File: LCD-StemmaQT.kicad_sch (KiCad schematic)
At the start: 18 parts, among them J101 StemmaQT, J102 LCD, J103 BL enable, Q101 MMBT3904, U101 PCF8574TS

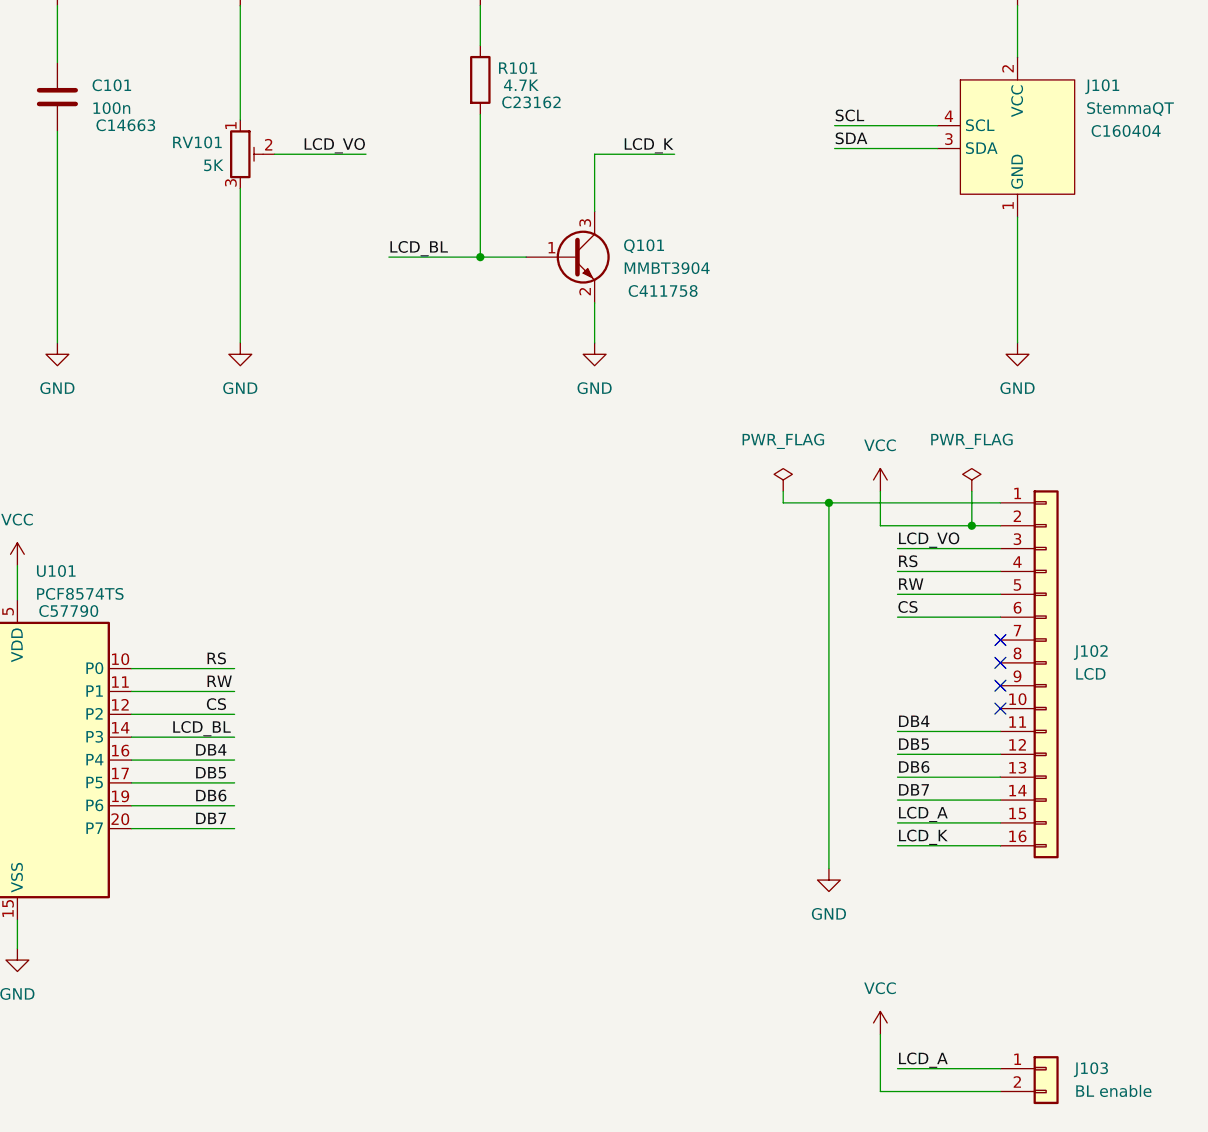
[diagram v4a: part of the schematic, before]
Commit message: Added second StemmaQT port
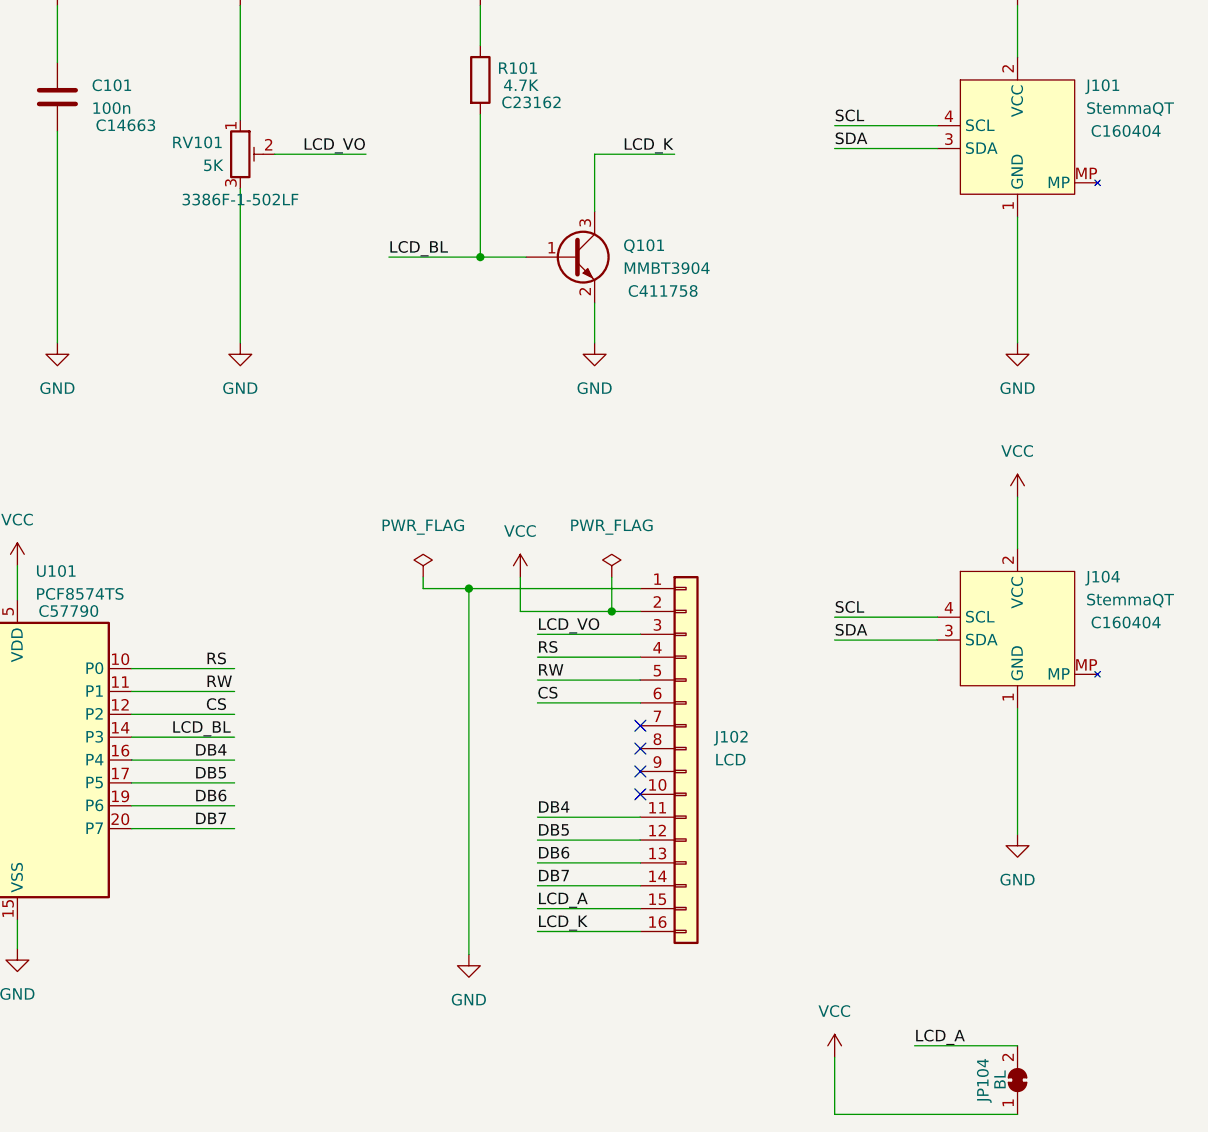
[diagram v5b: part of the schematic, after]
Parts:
- removed J103: BL enable, Connector_PinHeader_2.54mm:PinHeader_1x02_P2.54mm_Horizontal, symbol Connector_Generic:Conn_01x02
- added J104: StemmaQT, Connector_JST:JST_SH_SM04B-SRSS-TB_1x04-1MP_P1.00mm_Horizontal, symbol Resterampe:StemmaQT
- added JP104: BL, Jumper:SolderJumper-2_P1.3mm_Bridged_Pad1.0x1.5mm, symbol Jumper:SolderJumper_2_Bridged
- RV101: DigiKey (none) -> 3386F-1-502LF
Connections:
- net GND: now also J104.1 (GND)
- net LCD_A: now also JP104.2 (B)
- net SCL: now also J104.4 (SCL)
- net SDA: now also J104.3 (SDA)
- net VCC: now also J104.2 (VCC), JP104.1 (A)
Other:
- moved on the sheet: J102
